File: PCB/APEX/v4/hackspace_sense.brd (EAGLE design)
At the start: 77.5 x 27.9 mm, 9 parts

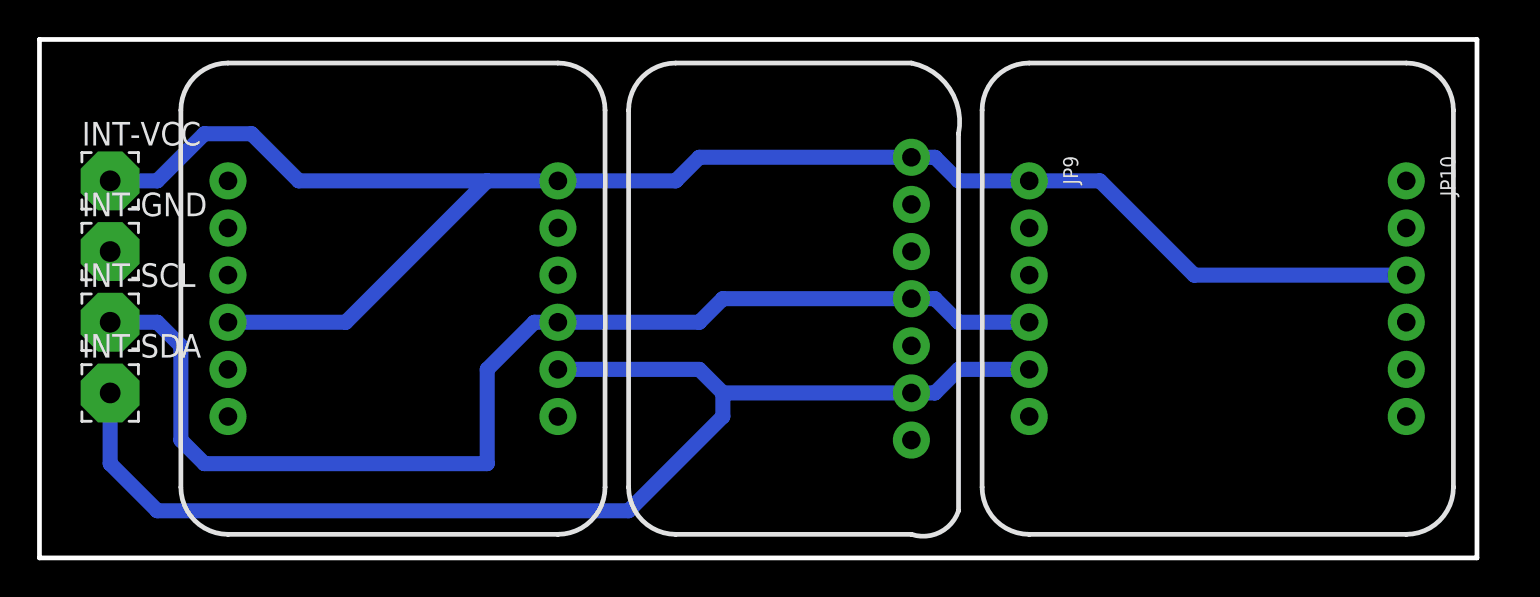
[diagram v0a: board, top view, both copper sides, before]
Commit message: increase trace widths
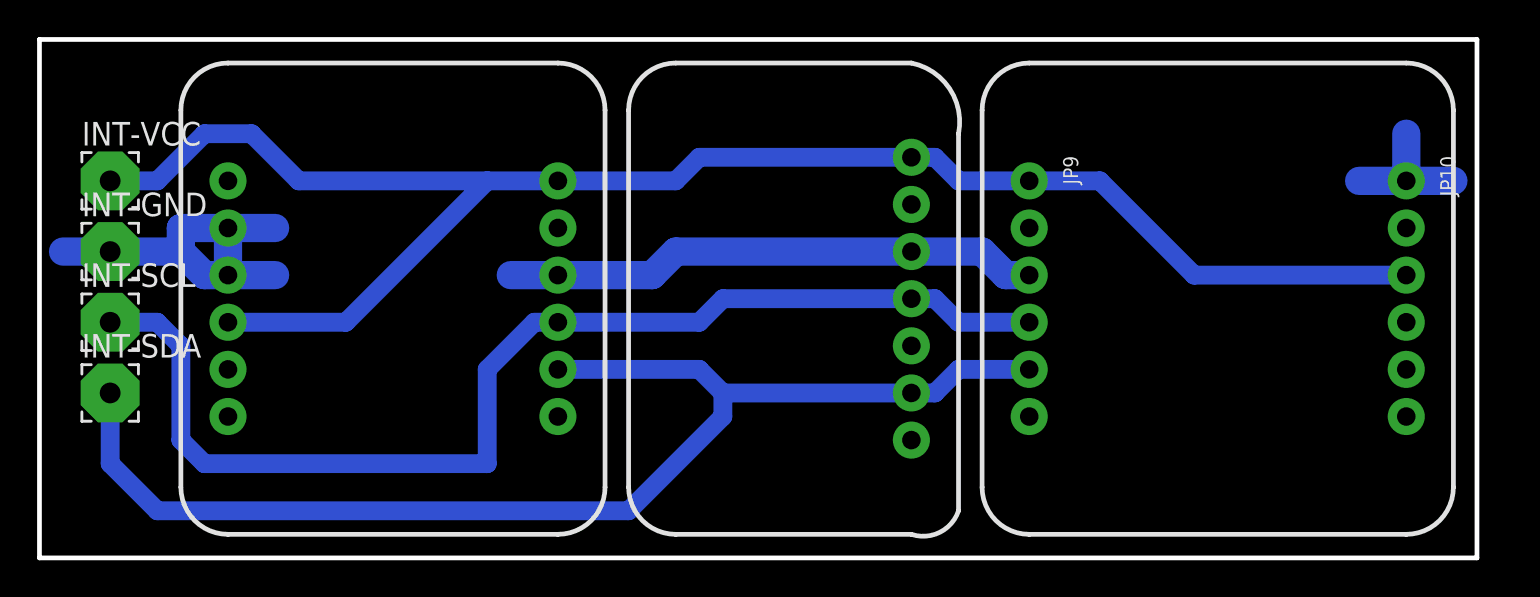
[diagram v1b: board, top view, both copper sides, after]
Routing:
- net GND: track 0.00 -> 57.5 mm

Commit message: add labels
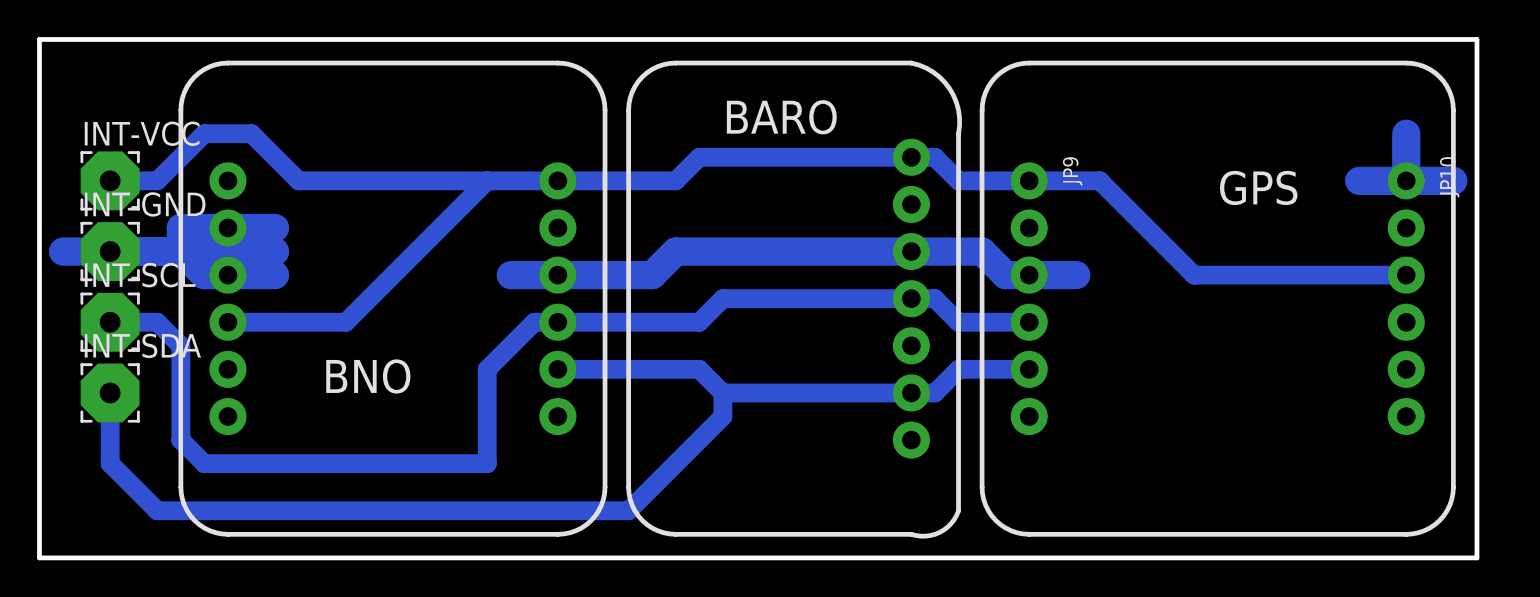
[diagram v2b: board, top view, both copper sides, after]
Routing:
- net GND: track 57.5 -> 68.9 mm
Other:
- board text added: "BARO"
- board text added: "BNO"
- board text added: "GPS"
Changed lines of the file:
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@@
 <dimension x1="27.94" y1="8.89" x2="105.41" y2="8.89" x3="66.675" y3="5.08" textsize="1.778" textratio="15" layer="49" width="0.254"/>
 <dimension x1="27.94" y1="36.83" x2="27.94" y2="8.89" x3="25.4" y3="22.86" textsize="1.778" textratio="15" layer="49" width="0.254"/>
+<text x="43.18" y="17.78" size="1.778" layer="21" font="vector" ratio="15">BNO</text>
+<text x="64.77" y="31.75" size="1.778" layer="21" font="vector" ratio="15">BARO</text>
+<text x="91.44" y="27.94" size="1.778" layer="21" font="vector" ratio="15">GPS</text>
 </plain>
 <attributes>
@@
 <wire x1="101.6" y1="29.21" x2="101.6" y2="31.75" width="1.524" layer="16"/>
 <wire x1="101.6" y1="29.21" x2="104.14" y2="29.21" width="1.524" layer="16"/>
+<wire x1="81.28" y1="24.13" x2="83.82" y2="24.13" width="1.524" layer="16"/>
+<wire x1="31.75" y1="25.4" x2="40.64" y2="25.4" width="1.524" layer="16"/>
 </signal>
 <signal name="VCC">

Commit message: embiggen pads
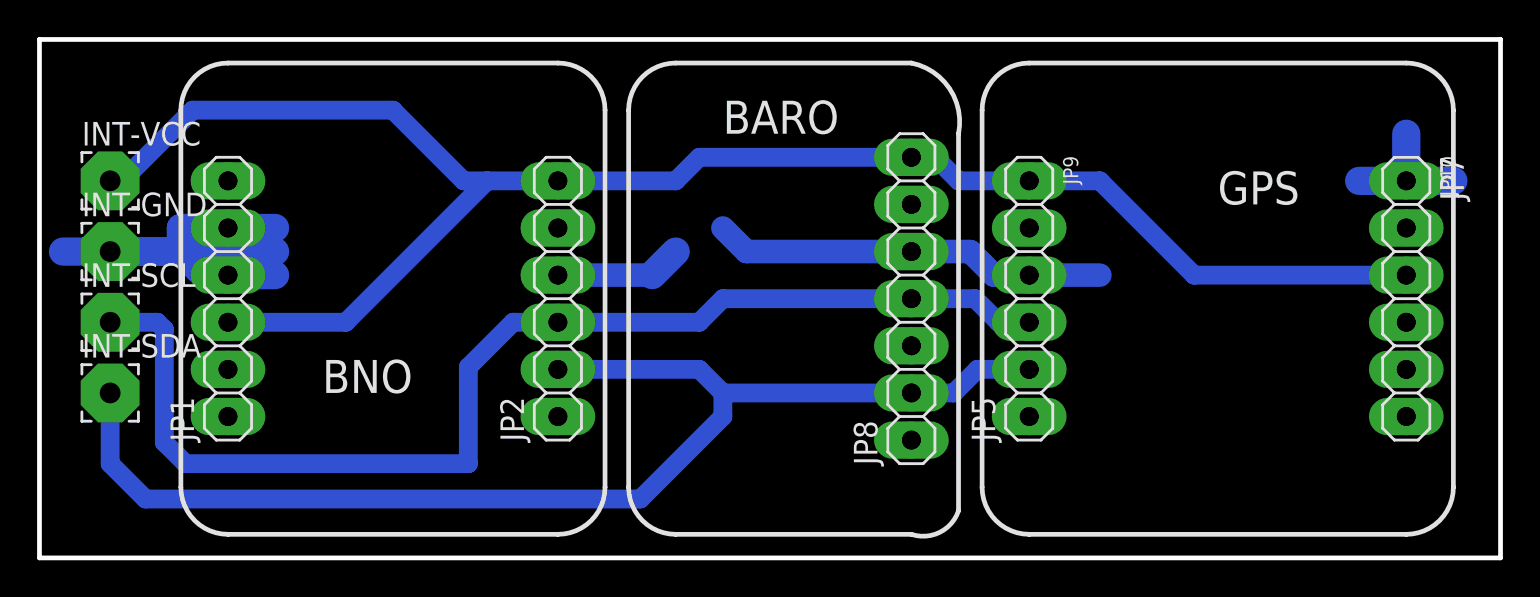
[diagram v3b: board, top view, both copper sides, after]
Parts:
- added JP1, JP2, JP5, JP7: (no value), pinhead:1X06
- added JP8: (no value), pinhead:1X07
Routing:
- net GND: track 68.9 -> 65.6 mm
- net VCC: track 92.2 -> 93.3 mm
- net SCL: track 62.8 -> 63.5 mm
- net SDA: track 67.7 -> 67.2 mm
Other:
- board size 77.5 x 27.9 mm -> 78.7 x 27.9 mm
